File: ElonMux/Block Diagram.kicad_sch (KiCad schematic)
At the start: 0 parts

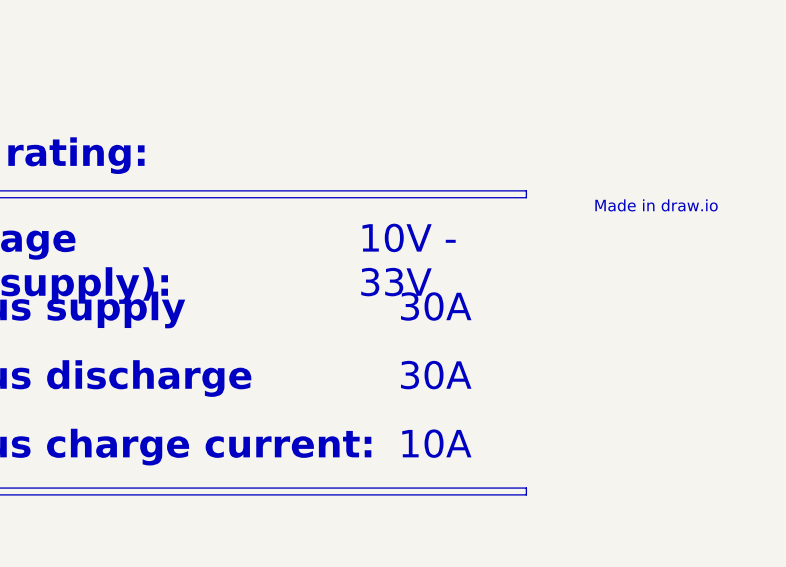
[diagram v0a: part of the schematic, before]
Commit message: Done with changes of v1.1, need to final check and order
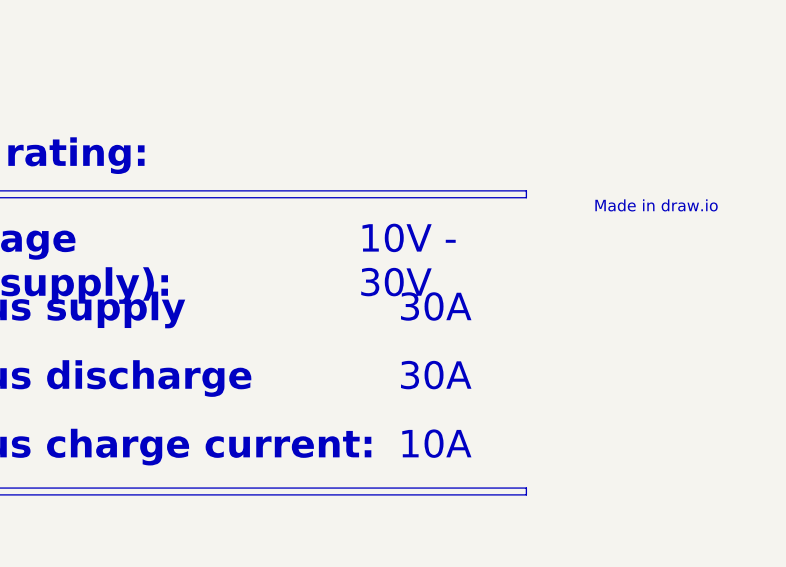
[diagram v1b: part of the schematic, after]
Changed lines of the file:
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@@
 	(title_block
 		(title "Block Diagram")
-		(date "Last Modified Date")
+		(date "2025-06-17")
 		(rev "${REVISION}")
 		(company "${COMPANY}")
@@
 		)
 	)
-	(text_box "10V - 33V"
+	(text_box "10V - 30V"
 		(exclude_from_sim no)
 		(at 236.22 248.285 0)
@@
 		(stroke
 			(width -0.0001)
-			(type default)
+			(type solid)
 		)
 		(fill
@@
 			"YmpRc3ZxMnlWZXcrb0JVb283Wi9WNTRMcHNqejB1Y1k3dUZmVAAAAAAAAAAAAAAAAAAAAAAAAAAA"
 			"AAAAAAAAAAAAAAAAAAAAAAAAAAAAAAAAAAAAAAAAAAAAAAAAAAAAAAAAAAAAAAAAAAAAAAAAAAAA"
+			"AAAAAAAAAAAAAAAAAAAAAAAAAAAAAAAAAAAAAAAAAAAAAAAAAAAAAAAAAAAAAAAAAAAAAAAAAAAA"
+			"AAAAAAAAAAAAAAAAAAAAAAAAAAAAAAAAAAAAAAAAAAAAAAAAAAAAAAAAAAAAAAAAAAAAAAAAAAAA"
+			"AAAAAAAAAAAAAAAAAAAAAAAAAAAAAAAAAAAAAAAAAAAAAAAAAAAAAAAAAAAAAAAAAAAAAAAAAAAA"
+			"AAAAAAAAAAAAAAAAAAAAAAAAAAAAAAAAAAAAAAAAAAAAAAAAAAAAAAAAAAAAAAAAAAAAAAAAAAAA"
+			"AAAAAAAAAAAAAAAAAAAAAAAAAAAAAAAAAAAAAAAAAAAAAAAAAAAAAAAAAAAAAAAAAAAAAAAAAAAA"
+			"AAAAAAAAAAAAAAAAAAAAAAAAAAAAAAAAAAAAAAAAAAAAAAAAAAAAAAAAAAAAAAAAAAAAAAAAAAAA"
+			"AAAAAAAAAAAAAAAAAAAAAAAAAAAAAAAAAAAAAAAAAAAAAAAAAAAAAAAAAAAAAAAAAAAAAAAAAAAA"
+			"AAAAAAAAAAAAAAAAAAAAAAAAAAAAAAAAAAAAAAAAAAAAAAAAAAAAAAAAAAAAAAAAAAAAAAAAAAAA"
+			"AAAAAAAAAAAAAAAAAAAAAAAAAAAAAAAAAAAAAAAAAAAAAAAAAAAAAAAAAAAAAAAAAAAAAAAAAAAA"
+			"AAAAAAAAAAAAAAAAAAAAAAAAAAAAAAAAAAAAAAAAAAAAAAAAAAAAAAAAAAAAAAAAAAAAAAAAAAAA"
+			"AAAAAAAAAAAAAAAAAAAAAAAAAAAAAAAAAAAAAAAAAAAAAAAAAAAAAAAAAAAAAAAAAAAAAAAAAAAA"
+			"AAAAAAAAAAAAAAAAAAAAAAAAAAAAAAAAAAAAAAAAAAAAAAAAAAAAAAAAAAAAAAAAAAAAAAAAAAAA"
+			"AAAAAAAAAAAAAAAAAAAAAAAAAAAAAAAAAAAAAAAAAAAAAAAAAAAAAAAAAAAAAAAAAAAAAAAAAAAA"
+			"AAAAAAAAAAAAAAAAAAAAAAAAAAAAAAAAAAAAAAAAAAAAAAAAAAAAAAAAAAAAAAAAAAAAAAAAAAAA"
+			"AAAAAAAAAAAAAAAAAAAAAAAAAAAAAAAAAAAAAAAAAAAAAAAAAAAAAAAAAAAAAAAAAAAAAAAAAAAA"
+			"AAAAAAAAAAAAAAAAAAAAAAAAAAAAAAAAAAAAAAAAAAAAAAAAAAAAAAAAAAAAAAAAAAAAAAAAAAAA"
+			"AAAAAAAAAAAAAAAAAAAAAAAAAAAAAAAAAAAAAAAAAAAAAAAAAAAAAAAAAAAAAAAAAAAAAAAAAAAA"
+			"AAAAAAAAAAAAAAAAAAAAAAAAAAAAAAAAAAAAAAAAAAAAAAAAAAAAAAAAAAAAAAAAAAAAAAAAAAAA"
+			"AAAAAAAAAAAAAAAAAAAAAAAAAAAAAAAAAAAAAAAAAAAAAAAAAAAAAAAAAAAAAAAAAHgAAAA4AAAA"
+			"WAAAAEYAAABGAAAAMQAAACsAAABjAAAAUwAAAGUAAABpAAAAUwAAAFMAAAB5AAAANgAAAEoAAABZ"
+			"AAAANAAAADQAAAA1AAAASgAAAGwAAABOAAAAcwAAADIAAABxAAAARAAAAC8AAAArAAAAcQAAAC8A"
+			"AAAvAAAAaQAAAHIAAAAzAAAAMwAAADMAAABqAAAAdAAAAHQAAAAyAAAATAAAAHIAAAB6AAAAeAAA"
+			"ADQAAAAwAAAAYgAAAEYAAAA0AAAAOAAAAC8AAAAvAAAAbgAAAGgAAABzAAAAdQAAAGUAAABXAAAA"
+			"VwAAAG0AAABlAAAATAAAAFQAAABCAAAAcAAAAFYAAABoAAAAZwAAAE0AAAByAAAAYQAAAHQAAABX"
+			"AAAAdgAAAGoAAABGAAAAYQAAADkAAAA0AAAAUgAAAGQAAAByAAAAUwAAAFkAAAA5AAAANgAAADgA"
+			"AABlAAAAWAAAAEgAAABhAAAAYQAAAGEAAABlAAAAbAAAAGoAAABrAAAAcwAAAGIAAAA4AAAASQAA"
+			"AE0AAABmAAAALwAAAEMAAABBAAAATwAAAE8AAABPAAAAQwAAAEEAAAB0AAAARwAAAEYAAAB4AAAA"
+			"LwAAAC8AAAAzAAAAMwAAAHgAAAA2AAAAUgAAAEoAAABrAAAAMQAAAEwAAABIAAAAQwAAAFMAAABC"
+			"AAAAUQAAAEYAAABRAAAASAAAAHYAAABWAAAAMQAAAFgAAABwAAAAdAAAAEQAAABvAAAASgAAAEUA"
+			"AABNAAAAaQAAAEwAAABnAAAATwAAAGQAAAB1AAAAWAAAAGoAAABvAAAAaAAAAEQAAAB3AAAASQAA"
+			"AEUAAABDAAAAQgAAAEEAAABnAAAAUQAAAEMAAABDAAAAdgAAAEEAAABnAAAAYQAAAG8AAAA1AAAA"
+			"TAAAAFUAAAB6AAAAOAAAAGkAAABKAAAAQQAAAFkAAABLAAAAaAAAAEEAAABFAAAAUQAAAGUAAABv"
+			"AAAASgAAAEkAAABOAAAAVAAAAGUAAABuAAAAdQAAAFQAAABYAAAAegAAAHUAAABLAAAARwAAAEIA"
+			"AABnAAAAWQAAADAAAABGAAAAUQAAAEMAAABCAAAAQQAAAGcAAABRAAAASwAAAEwAAABoAAAAQQAA"
+			"AGQAAAAzAAAAZAAAADMAAABKAAAASQAAAE4AAABVAAAAawAAAG0AAABkAAAANwAAADMAAABvAAAA"
+			"ZAAAAGkAAABHAAAAYQAAAEIAAABTAAAAOAAAAEoAAAB0AAAATgAAACsAAABnAAAAUQAAAHEAAABK"
+			"AAAARwAAAEMAAABBAAAAUwAAAG8AAABXAAAAYQAAAHIAAABWAAAAUQAAAEMAAAAAAAAAAAAAAAAA"
+			"AAAAAAAAAAAAAAAAAAAAAAAAAAAAAAAAAAAAAAAAAAAAAAAAAAAAAAAAAAAAAAAAAAAAAAAAAAAA"
+			"AAAAAAAAAAAAAAAAAAAAAAAAAAAAAAAAAAAAAAAAAAAAAAAAAAAAAAAAAAAAAAAAAAAAAAAAAAAA"
+			"AAAAAAAAAAAAAAAAAAAAAAAAAAAAAAAAAAAAAAAAAAAAAAAAAAAAAAAAAAAAAAAAAAAAAAAAAAAA"
+			"AAAAAAAAAAAAAAAAAAAAAAAAAAAAAAAAAAAAAAAAAAAAAAAAAAAAAAAAAAAAAAAAAAAAAAAAAAAA"
+			"AAAAAAAAAAAAAAAAAAAAAAAAAAAAAAAAAAAAAAAAAAAAAAAAAAAAAAAAAAAAAAAAAAAAAAAAAAAA"
+			"AAAAAAAAAAAAAAAAAAAAAAAAAAAAAAAAAAAAAAAAAAAAAAAAAAAAAAAAAAAAAAAAAAAAAAAAAAAA"
+			"AAAAAAAAAAAAAAAAAAAAAAAAAAAAAAAAAAAAAAAAAAAAAAAAAAAAAAAAAAAAAAAAAAAAAAAAAAAA"
+			"AAAAAAAAAAAAAAAAAAAAAAAAAAAAAAAAAAAAAAAAAAAAAAAAAAAAAAAAAAAAAAAAAAAAAAAAAAAA"
+			"AAAAAAAAAAAAAAAAAAAAAAAAAAAAAAAAAAAAAAAAAAAAAAAAAAAAAAAAAAAAAAAAAAAAAAAAAAAA"
+			"AAAAAAAAAAAAAAAAAAAAAAAAAAAAAAAAAAAAAAAAAAAAAAAAAAAAAAAAAAAAAAAAAAAAAAAAAAAA"
+			"AAAAAAAAAAAAAAAAAAAAAAAAAAAAAAAAAAAAAAAAAAAAAAAAAAAAAAAAAAAAAAAAAAAAAAAAAAAA"
+			"AAAAAAAAAAAAAAAAAAAAAAAAAAAAAAAAAAAAAAAAAAAAAAAAAAAAAAAAAAAAAAAAAAAAAAAAAAAA"
+			"AAAAAAAAAAAAAAAAAAAAAAAAAAAAAAAAAAAAAAAAAAAAAAAAAAAAAAAAAAAAAAAAAAAAAAAAAAAA"
+			"AAAAAAAAAAAAAAAAAAAAAAAAAAAAAAAAAAAAAAAAAAAAAAAAAAAAAAAAAAAAAAAAAAAAAAAAAAAA"
+			"AAAAAAAAAAAAAAAAAAAAAAAAAAAAAAAAAAAAAAAAAAAAAAAAAAAAAAAAAAAAAAAAAAAAAAAAAAAA"
+			"AAAAAAAAAAAAAAAAAAAAAAAAAAAAAAAAAAAAAAAAAAAAAAAAAAAAAAAAAAAAAAAAAAAAAAAAAAAA"
+			"AAAAAAAAAAAAAAAAAAAAAAAAAAAAAAAAAAAAAAAAAAAAAAAAAAAAAAAAAAAAAAAAAAAAAAAAAAAA"
 			"AAAAAAAAAAAAAAAAAAAAAAAAAAAAAAAAAAAAAAAAAAAAAAAAAAAAAAAAAAAAAA=="

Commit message: Finished V1.1, maybe extra cleaning needed of some details in the doc
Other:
- note added: "OUT OF DATE"
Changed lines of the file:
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@@
 	(title_block
 		(title "Block Diagram")
-		(date "2025-06-17")
+		(date "2025-07-24")
 		(rev "${REVISION}")
 		(company "${COMPANY}")
@@
 	)
 	(rectangle
+		(start 299.085 199.39)
+		(end 375.92 219.075)
+		(stroke
+			(width 0.508)
+			(type solid)
+			(color 0 0 0 1)
+		)
+		(fill
+			(type color)
+			(color 255 0 0 1)
+		)
+	)
+	(rectangle
 		(start 174.625 247.015)
 		(end 257.175 247.777)
@@
 		)
 	)
+	(text "OUT OF DATE"
+		(exclude_from_sim no)
+		(at 337.058 210.566 0)
+		(effects
+			(font
+				(size 7.62 7.62)
+				(thickness 1.524)
+				(bold yes)
+				(color 255 255 255 1)
+			)
+		)
+	)
 	(text "Made in draw.io"
 		(exclude_from_sim no)
@@
 		)
 	)
-	(text_box "30A"
+	(text_box "40A"
 		(exclude_from_sim no)
 		(at 234.95 255.905 0)
@@
 		(stroke
 			(width -0.0001)
-			(type default)
+			(type solid)
 		)
 		(fill
@@
 		)
 	)
-	(text_box "30A"
+	(text_box "40A"
 		(exclude_from_sim no)
 		(at 234.95 263.525 0)
@@
 		(stroke
 			(width -0.0001)
-			(type default)
+			(type solid)
 		)
 		(fill
@@
 			"AAAAAAAAAAAAAAAAAAAAAAAAAAAAAAAAAAAAAAAAAAAAAAAAAAAAAAAAAAAAAAAAAAAAAAAAAAAA"
 			"AAAAAAAAAAAAAAAAAAAAAAAAAAAAAAAAAAAAAAAAAAAAAAAAAAAAAAAAAAAAAAAAAAAAAAAAAAAA"
+			"AAAAAAAAAAAAAAAAAAAAAAAAAAAAAAAAAAAAAAAAAAAAAAAAAAAAAAAAAAAAAAAAAAAAAAAAAAAA"
+			"AAAAAAAAAAAAAAAAAAAAAAAAAAAAAAAAAAAAAAAAAAAAAAAAAAAAAAAAAAAAAAAAAAAAAAAAAAAA"
+			"AAAAAAAAAAAAAAAAAAAAAAAAAAAAAAAAAAAAAAAAAAAAAAAAAAAAAAAAAAAAAAAAAAAAAAAAAAAA"
+			"AAAAAAAAAAAAAAAAAAAAAAAAAAAAAAAAAAAAAAAAAAAAAAAAAAAAAAAAAAAAAAAAAAAAAAAAAAAA"
+			"AAAAAAAAAAAAAAAAAAAAAAAAAAAAAAAAAAAAAAAAAAAAAAAAAAAAAAAAAAAAAAAAAAAAAAAAAAAA"
+			"AAAAAAAAAAAAAAAAAAAAAAAAAAAAAAAAAAAAAAAAAAAAAAAAAAAAAAAAAAAAAAAAAAAAAAAAAAAA"
+			"AAAAAAAAAAAAAAAAAAAAAAAAAAAAAAAAAAAAAAAAAAAAAAAAAAAAAAAAAAAAAAAAAAAAAAAAAAAA"
+			"AAAAAAAAAAAAAAAAAAAAAAAAAAAAAAAAAAAAAAAAAAAAAAAAAAAAAAAAAAAAAAAAAAAAAAAAAAAA"
+			"AAAAAAAAAAAAAAAAAAAAAAAAAAAAAAAAAAAAAAAAAAAAAAAAAAAAAAAAAAAAAAAAAAAAAAAAAAAA"
+			"AAAAAAAAAAAAAAAAAAAAAAAAAAAAAAAAAAAAAAAAAAAAAAAAAAAAAAAAAAAAAAAAAAAAAAAAAAAA"
+			"AAAAAAAAAAAAAAAAAAAAAAAAAAAAAAAAAAAAAAAAAAAAAAAAAAAAAAAAAAAAAAAAAAAAAAAAAAAA"
+			"AAAAAAAAAAAAAAAAAAAAAAAAAAAAAAAAAAAAAAAAAAAAAAAAAAAAAAAAAAAAAAAAAAAAAAAAAAAA"
+			"AAAAAAAAAAAAAAAAAAAAAAAAAAAAAAAAAAAAAAAAAAAAAAAAAAAAAAAAAAAAAAAAAAAAAAAAAAAA"
+			"AAAAAAAAAAAAAAAAAAAAAAAAAAAAAAAAAAAAAAAAAAAAAAAAAAAAAAAAAAAAAAAAAAAAAAAAAAAA"
+			"AAAAAAAAAAAAAAAAAAAAAAAAAAAAAAAAAAAAAAAAAAAAAAAAAAAAAAAAAAAAAAAAAAAAAAAAAAAA"
+			"AAAAAAAAAAAAAAAAAAAAAAAAAAAAAAAAAAAAAAAAAAAAAAAAAAAAAAAAAAAAAAAAAAAAAAAAAAAA"
+			"AAAAAAAAAAAAAAAAAAAAAAAAAAAAAAAAAAAAAAAAAAAAAAAAAAAAAAAAAAAAAAAAAAAAAAAAAAAA"
+			"AAAAAAAAAAAAAAAAAAAAAAAAAAAAAAAAAAAAAAAAAAAAAAAAAAAAAAAAAAAAAAAAAAAAAAAAAAAA"

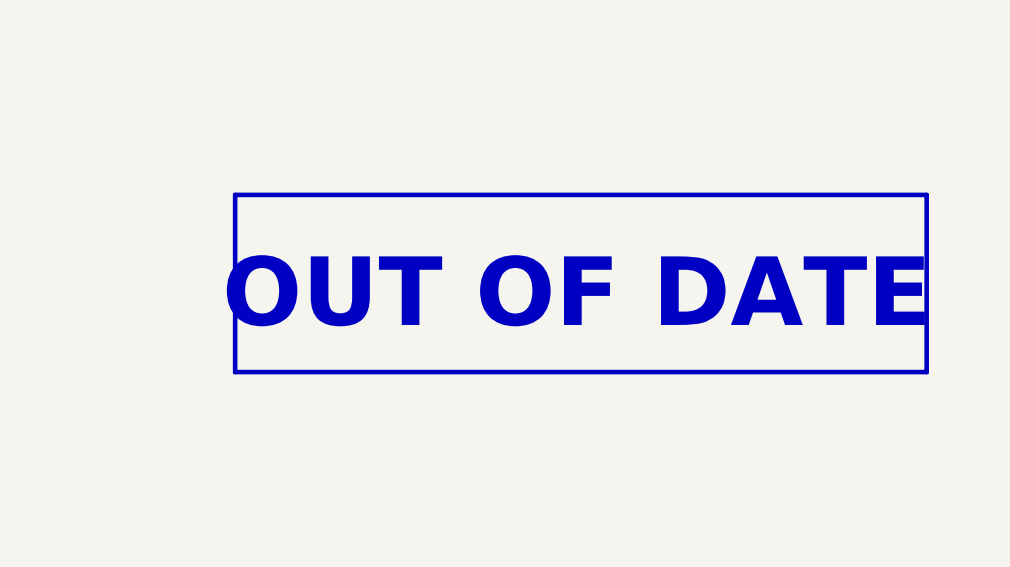
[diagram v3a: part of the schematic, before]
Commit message: Cleaned README, updated block diagram
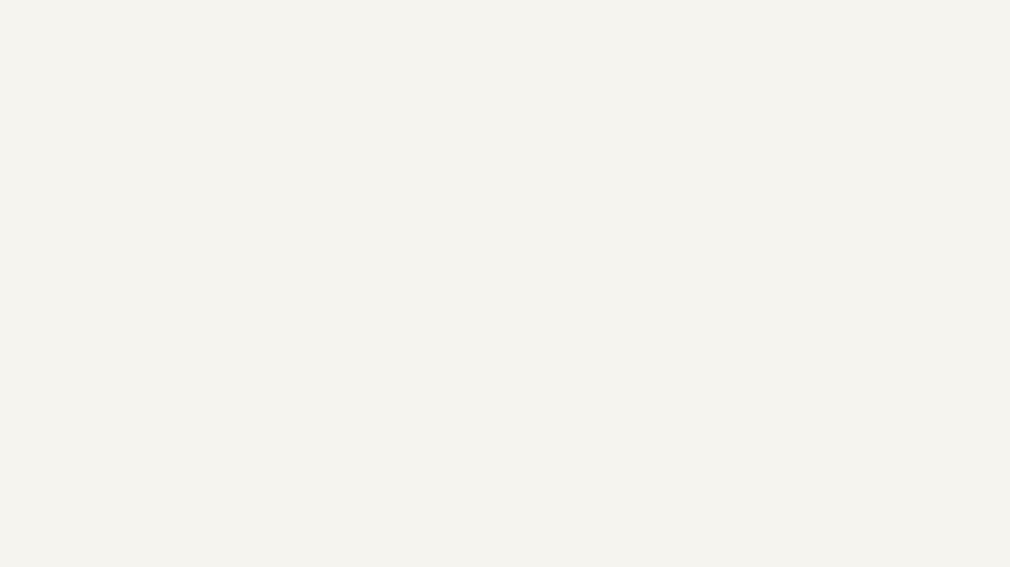
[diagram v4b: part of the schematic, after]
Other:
- note removed: "OUT OF DATE"
